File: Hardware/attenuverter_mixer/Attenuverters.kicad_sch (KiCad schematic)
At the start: 36 parts, among them J1 thonkiconn, J3 thonkiconn, J4 thonkiconn, J8 thonkiconn, J9 thonkiconn, U1 TL074, U2 TL074

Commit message: created fabrication output
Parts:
- C1, C13, C14, C2, C5, C6: LCSC (none) -> C105622
- R1, R2, R4, R5, R7, R8: LCSC (none) -> C14675
- R10, R11, R16, R17, R22, R6: LCSC (none) -> C98220
- R13, R14, R21: LCSC (none) -> C137760
- R19, R20: LCSC (none) -> C83144
- U1, U2: LCSC (none) -> C96507
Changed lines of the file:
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@@
     (stroke (width 0) (type default))
   )
-  (wire (pts (xy 121.92 111.76) (xy 121.92 110.49))
+  (wire (pts (xy 121.92 110.49) (xy 121.92 111.76))
     (stroke (width 0) (type default))
   )
@@
       (effects (font (size 1.27 1.27)) hide)
     )
+    (property "LCSC" " C137760" (at 113.03 45.72 0)
+      (effects (font (size 1.27 1.27)) hide)
+    )
     (pin "1")
     (pin "2")
@@
     )
     (property "MPN" "RC0603FR-0710KL" (at 100.33 59.69 0)
+      (effects (font (size 1.27 1.27)) hide)
+    )
+    (property "LCSC" "C98220" (at 100.33 59.69 0)
       (effects (font (size 1.27 1.27)) hide)
     )
@@
       (effects (font (size 1.27 1.27)) hide)
     )
+    (property "LCSC" " C137760" (at 111.76 91.44 0)
+      (effects (font (size 1.27 1.27)) hide)
+    )
     (pin "1")
     (pin "2")
@@
       (effects (font (size 1.27 1.27)) hide)
     )
+    (property "LCSC" "C98220" (at 132.08 135.89 0)
+      (effects (font (size 1.27 1.27)) hide)
+    )
     (pin "1")
     (pin "2")
@@
       (effects (font (size 1.27 1.27)) hide)
     )
+    (property "LCSC" "C14675" (at 81.28 45.72 0)
+      (effects (font (size 1.27 1.27)) hide)
+    )
     (pin "1")
     (pin "2")
@@
       (effects (font (size 1.27 1.27)) hide)
     )
+    (property "LCSC" "C98220" (at 130.81 91.44 0)
+      (effects (font (size 1.27 1.27)) hide)
+    )
     (pin "1")
     (pin "2")
@@
     )
     (property "MPN" "RC0603FR-07100KL" (at 63.5 147.32 0)
+      (effects (font (size 1.27 1.27)) hide)
+    )
+    (property "LCSC" "C14675" (at 63.5 147.32 0)
       (effects (font (size 1.27 1.27)) hide)
     )
@@
       (effects (font (size 1.27 1.27)) hide)
     )
+    (property "LCSC" "C14675" (at 62.23 57.15 0)
+      (effects (font (size 1.27 1.27)) hide)
+    )
     (pin "1")
     (pin "2")
@@
       (effects (font (size 1.27 1.27)) hide)
     )
+    (property "LCSC" "C14675" (at 81.28 91.44 0)
+      (effects (font (size 1.27 1.27)) hide)
+    )
     (pin "1")
     (pin "2")
@@
     )
     (property "MPN" "CC0603JRNPO9BN470" (at 130.81 81.28 0)
+      (effects (font (size 1.27 1.27)) hide)
+    )
+    (property "LCSC" "C105622" (at 130.81 81.28 0)
       (effects (font (size 1.27 1.27)) hide)
     )
@@
     )
     (property "MPN" "TL074CPWR" (at 132.08 152.4 0)
+      (effects (font (size 1.27 1.27)) hide)
+    )
+    (property "LCSC" "C96507" (at 132.08 152.4 0)
       (effects (font (size 1.27 1.27)) hide)
     )
@@
       (effects (font (size 1.27 1.27)) hide)
     )
+    (property "LCSC" " C137760" (at 113.03 135.89 0)
+      (effects (font (size 1.27 1.27)) hide)
+    )
     (pin "1")
     (pin "2")
@@
       (effects (font (size 1.27 1.27)) hide)
     )
+    (property "LCSC" "C98220" (at 101.6 105.41 0)
+      (effects (font (size 1.27 1.27)) hide)
+    )
     (pin "1")
     (pin "2")
@@
     )
     (property "MPN" "TL074CPWR" (at 130.81 62.23 0)
+      (effects (font (size 1.27 1.27)) hide)
+    )
+    (property "LCSC" "C96507" (at 130.81 62.23 0)
       (effects (font (size 1.27 1.27)) hide)
     )
@@
       (effects (font (size 1.27 1.27)) hide)
     )
+    (property "LCSC" "C83144" (at 154.94 107.95 0)
+      (effects (font (size 1.27 1.27)) hide)
+    )
     (pin "1")
     (pin "2")
@@
     )
     (property "MPN" "TL074CPWR" (at 83.82 149.86 0)
+      (effects (font (size 1.27 1.27)) hide)
+    )
+    (property "LCSC" "C96507" (at 83.82 149.86 0)
       (effects (font (size 1.27 1.27)) hide)
     )
@@
       (effects (font (size 1.27 1.27)) hide)
     )
+    (property "LCSC" "C14675" (at 62.23 102.87 0)
+      (effects (font (size 1.27 1.27)) hide)
+    )
     (pin "1")
     (pin "2")
@@
     )
     (property "MPN" "TL074CPWR" (at 82.55 105.41 0)
+      (effects (font (size 1.27 1.27)) hide)
+    )
+    (property "LCSC" "C96507" (at 82.55 105.41 0)
       (effects (font (size 1.27 1.27)) hide)
     )
@@
       (effects (font (size 1.27 1.27)) hide)
     )
+    (property "LCSC" "C105622" (at 132.08 125.73 0)
+      (effects (font (size 1.27 1.27)) hide)
+    )
     (pin "1")
     (pin "2")
@@
       (effects (font (size 1.27 1.27)) hide)
     )
+    (property "LCSC" "C98220" (at 130.81 45.72 0)
+      (effects (font (size 1.27 1.27)) hide)
+    )
     (pin "1")
     (pin "2")
@@
     )
     (property "MPN" "RC0603FR-07100KL" (at 82.55 135.89 0)
+      (effects (font (size 1.27 1.27)) hide)
+    )
+    (property "LCSC" "C14675" (at 82.55 135.89 0)
       (effects (font (size 1.27 1.27)) hide)
     )
@@
       (effects (font (size 1.27 1.27)) hide)
     )
+    (property "LCSC" "C105622" (at 130.81 35.56 0)
+      (effects (font (size 1.27 1.27)) hide)
+    )
     (pin "1")
     (pin "2")
@@
       (effects (font (size 1.27 1.27)) hide)
     )
+    (property "LCSC" "C105622" (at 81.28 36.83 0)
+      (effects (font (size 1.27 1.27)) hide)
+    )
     (pin "1")
     (pin "2")
@@
       (effects (font (size 1.27 1.27)) hide)
     )
+    (property "LCSC" "C83144" (at 154.94 62.23 0)
+      (effects (font (size 1.27 1.27)) hide)
+    )
     (pin "1")
     (pin "2")
@@
       (effects (font (size 1.27 1.27)) hide)
     )
+    (property "LCSC" "C105622" (at 81.28 81.28 0)
+      (effects (font (size 1.27 1.27)) hide)
+    )
     (pin "1")
     (pin "2")
@@
     )
     (property "MPN" "TL074CPWR" (at 130.81 107.95 0)
+      (effects (font (size 1.27 1.27)) hide)
+    )
+    (property "LCSC" "C96507" (at 130.81 107.95 0)
       (effects (font (size 1.27 1.27)) hide)
     )
@@
       (effects (font (size 1.27 1.27)) hide)
     )
+    (property "LCSC" "C98220" (at 102.87 149.86 0)
+      (effects (font (size 1.27 1.27)) hide)
+    )
     (pin "1")
     (pin "2")
@@
     )
     (property "MPN" "TL074CPWR" (at 82.55 59.69 0)
+      (effects (font (size 1.27 1.27)) hide)
+    )
+    (property "LCSC" "C96507" (at 82.55 59.69 0)
       (effects (font (size 1.27 1.27)) hide)
     )
@@
       (effects (font (size 1.27 1.27)) hide)
     )
+    (property "LCSC" "C105622" (at 82.55 125.73 0)
+      (effects (font (size 1.27 1.27)) hide)
+    )

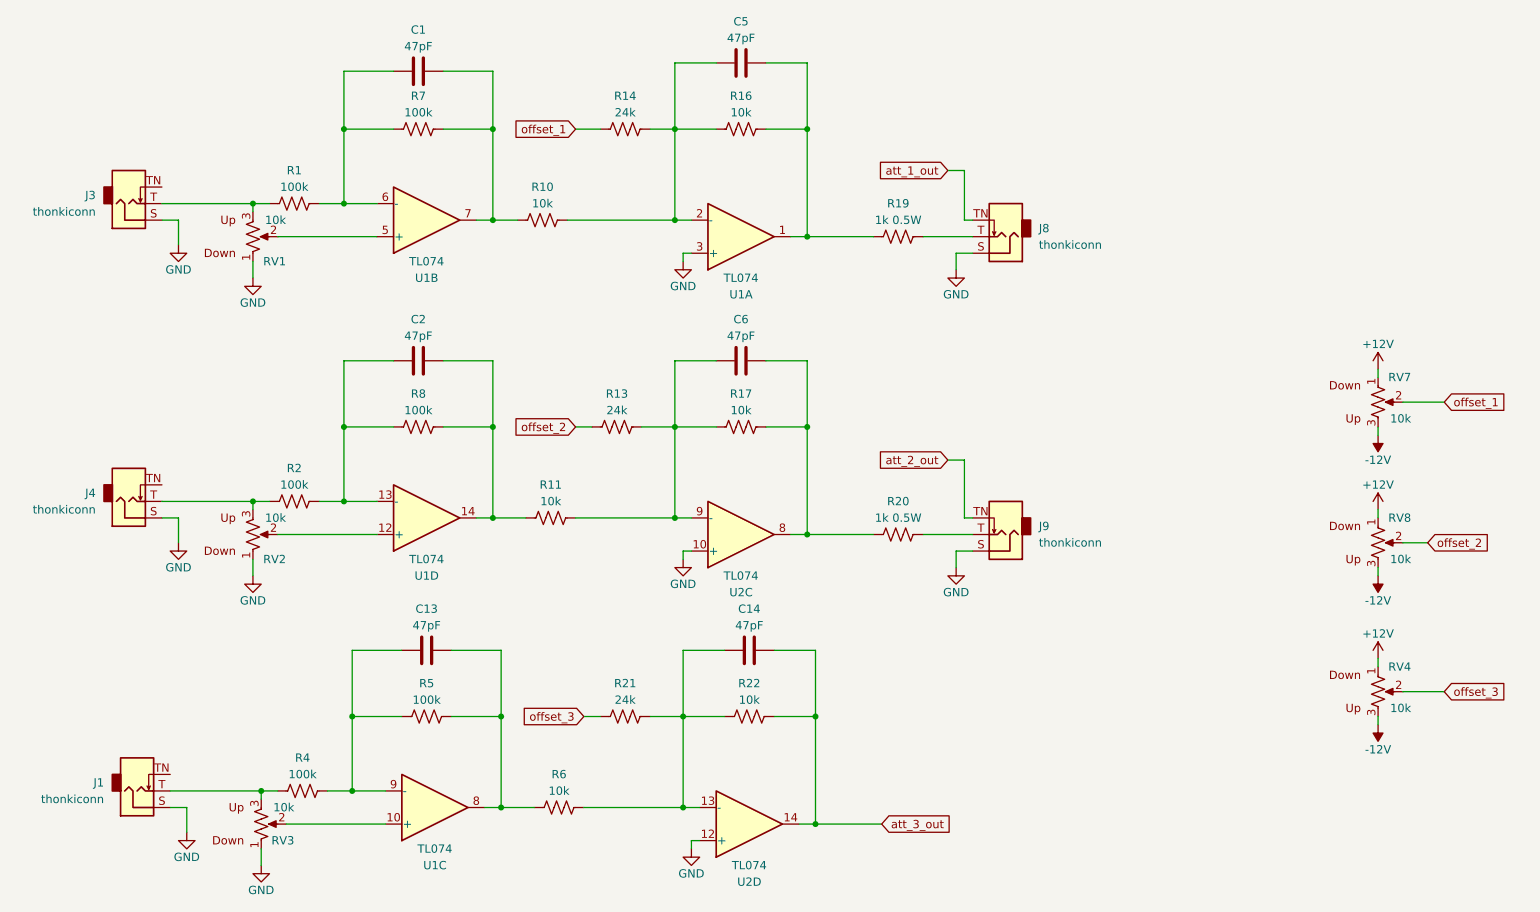
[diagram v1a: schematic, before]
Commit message: proto order
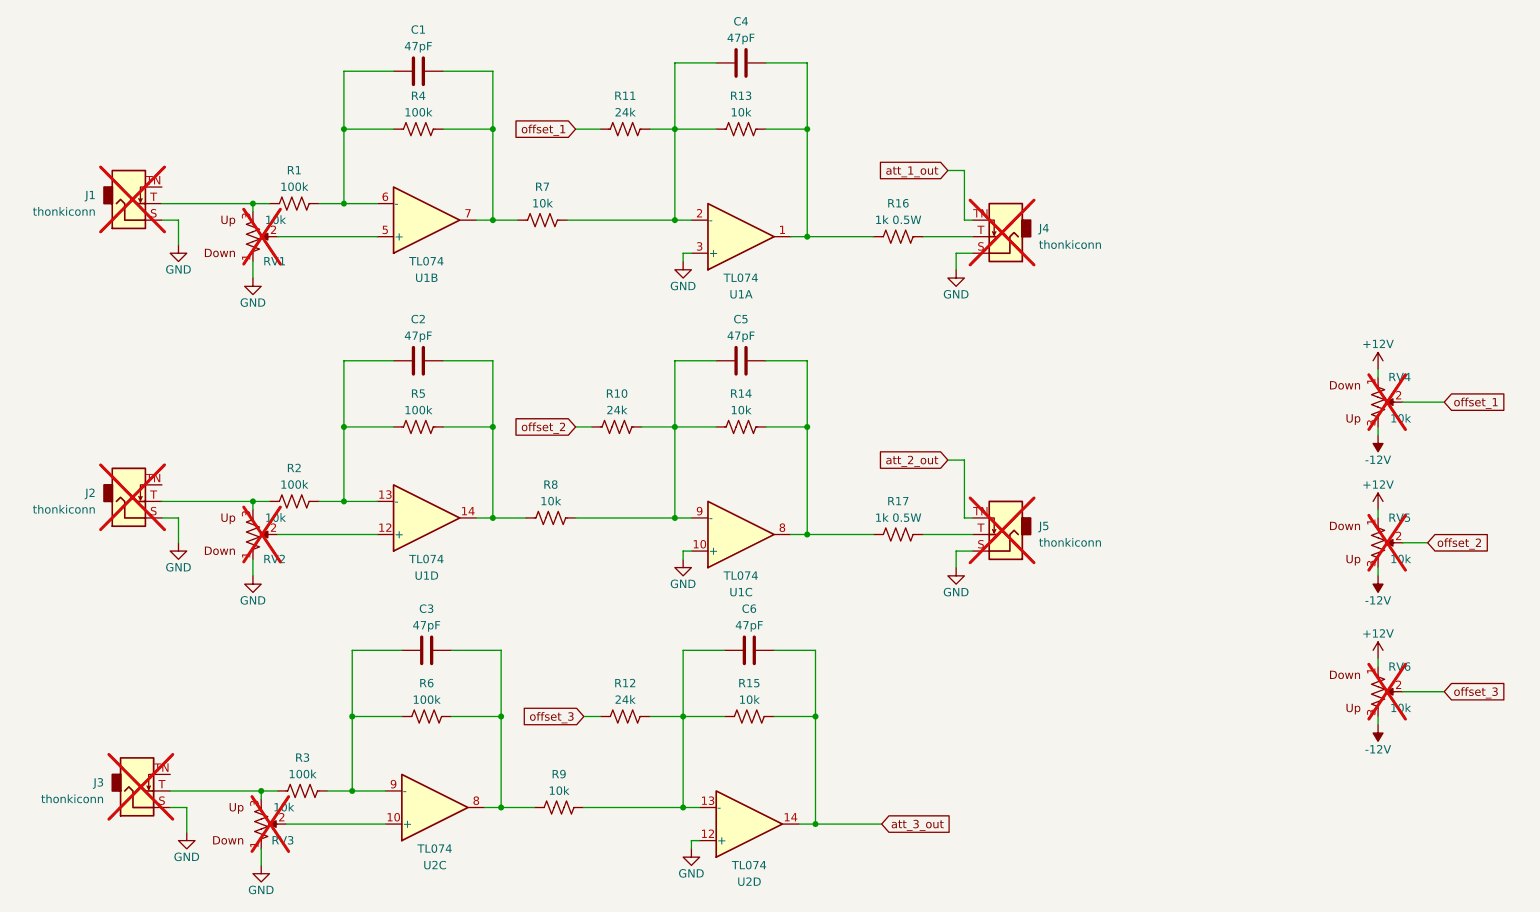
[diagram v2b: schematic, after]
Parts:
- J1: renamed from J3; now not fitted
- J2: renamed from J4; now not fitted
- J3: renamed from J1; now not fitted
- J4: renamed from J8; now not fitted
- J5: renamed from J9; now not fitted
- RV1, RV2, RV3: now not fitted
- RV4: renamed from RV7; now not fitted
- RV5: renamed from RV8; now not fitted
- RV6: renamed from RV4; now not fitted
- renumbered C13 to C3, C5 to C4, C6 to C5, C14 to C6, R13 to R10, R14 to R11, R21 to R12, R16 to R13, R17 to R14, R22 to R15, R19 to R16, R20 to R17, R4 to R3, R7 to R4, R8 to R5, R5 to R6, R10 to R7, R11 to R8, R6 to R9, U2 to U1, U1 to U2
